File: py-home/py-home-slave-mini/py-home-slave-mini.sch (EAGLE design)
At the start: 20 parts, among them IC1 uln2308, K1 JS-M1-9V-4, K2 JS-M1-9V-4

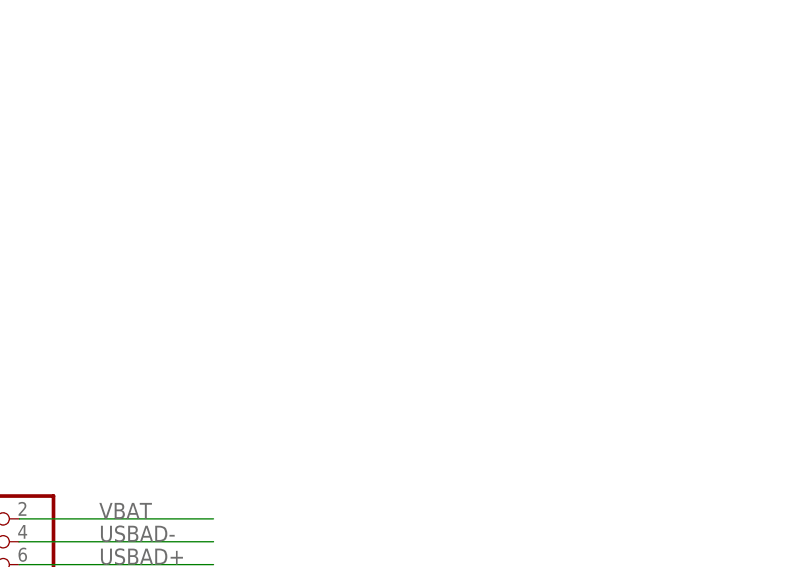
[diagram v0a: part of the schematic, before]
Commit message: aggiunto porta usb
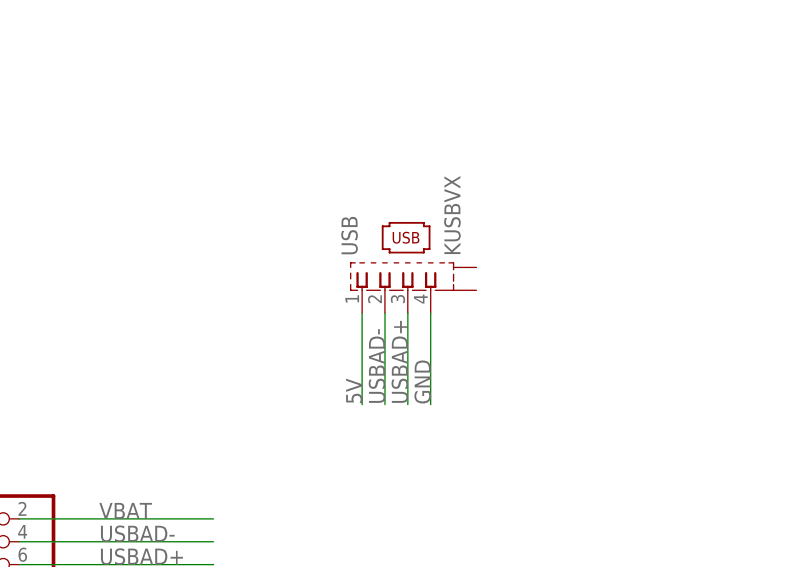
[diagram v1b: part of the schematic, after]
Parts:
- added USB: KUSBVX, con-kycon:KUSBVX
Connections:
- net 5V: now also USB.1
- net GND: now also USB.4
- net USBAD+: now also USB.3
- net USBAD-: now also USB.2
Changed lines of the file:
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@@
 <setting verticaltext="up"/>
 </settings>
-<grid distance="0.1" unitdist="inch" unit="inch" style="lines" multiple="1" display="no" altdistance="0.01" altunitdist="inch" altunit="inch"/>
+<grid distance="0.1" unitdist="inch" unit="inch" style="lines" multiple="1" display="yes" altdistance="0.01" altunitdist="inch" altunit="inch"/>
 <layers>
 <layer number="1" name="Top" color="4" fill="1" visible="no" active="no"/>
@@
 <part name="JP3" library="pinhead" deviceset="PINHD-2X3" device=""/>
 <part name="OUTPUT" library="con-phoenix-508" deviceset="MSTBA4" device=""/>
+<part name="USB" library="con-kycon" deviceset="KUSBVX" device=""/>
 </parts>
 <sheets>
@@
 <instance part="OUTPUT" gate="-3" x="93.98" y="168.91" rot="R270"/>
 <instance part="OUTPUT" gate="-4" x="88.9" y="168.91" rot="R270"/>
+<instance part="USB" gate="G$1" x="60.96" y="60.96" rot="R90"/>
 </instances>
 <busses>
@@
 <wire x1="12.7" y1="162.56" x2="19.05" y2="162.56" width="0.1524" layer="91"/>
 <label x="17.78" y="162.56" size="1.778" layer="95"/>
+</segment>
+<segment>
+<pinref part="USB" gate="G$1" pin="1"/>
+<wire x1="55.88" y1="55.88" x2="55.88" y2="45.72" width="0.1524" layer="91"/>
+<label x="55.88" y="45.72" size="1.778" layer="95" rot="R90"/>
 </segment>
 </net>
@@
 <label x="26.67" y="27.94" size="1.778" layer="95"/>
 </segment>
+<segment>
+<pinref part="USB" gate="G$1" pin="3"/>
+<wire x1="60.96" y1="55.88" x2="60.96" y2="45.72" width="0.1524" layer="91"/>
+<label x="60.96" y="45.72" size="1.778" layer="95" rot="R90"/>
+</segment>
 </net>
 <net name="USBAD-" class="0">
@@
 <wire x1="17.78" y1="30.48" x2="39.37" y2="30.48" width="0.1524" layer="91"/>
 <label x="26.67" y="30.48" size="1.778" layer="95"/>
+</segment>
+<segment>
+<pinref part="USB" gate="G$1" pin="2"/>
+<wire x1="58.42" y1="55.88" x2="58.42" y2="45.72" width="0.1524" layer="91"/>
+<label x="58.42" y="45.72" size="1.778" layer="95" rot="R90"/>
 </segment>
 </net>
@@
 <label x="-1.27" y="162.56" size="1.778" layer="95"/>
 </segment>
-</net>
+<segment>
+<pinref part="USB" gate="G$1" pin="4"/>
+<wire x1="63.5" y1="55.88" x2="63.5" y2="45.72" width="0.1524" layer="91"/>
+<label x="63.5" y="45.72" size="1.778" layer="95" rot="R90"/>
+</segment>
+</net>
